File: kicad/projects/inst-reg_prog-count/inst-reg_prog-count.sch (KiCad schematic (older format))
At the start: 0 parts

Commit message: Place components in schematic.
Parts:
- added C? (x5): C, symbol Device:C
- added J?: Conn_01x34_Male, symbol Connector:Conn_01x34_Male
- added J? (x2): Conn_01x08_Female, symbol Connector:Conn_01x08_Female
- added J? (x2): Conn_01x16_Female, symbol Connector:Conn_01x16_Female
- added J?: Conn_01x08_Male, symbol Connector:Conn_01x08_Male
- added J? (x5): Conn_01x01_Female, symbol Connector:Conn_01x01_Female
- added U? (x2): 74HCT161, symbol eight-bit-computer:74HCT161
- added U?: 74HCT245, symbol eight-bit-computer:74HCT245
- added U? (x7): 74HCT04, symbol 74xx:74HCT04
- added U?: 74HCT377, symbol eight-bit-computer:74HCT377

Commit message: Almost finished PC IR schematic.
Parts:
- removed J?: Conn_01x08_Female, symbol Connector:Conn_01x08_Female
- removed J?: Conn_01x16_Female, symbol Connector:Conn_01x16_Female
- removed J?: Conn_01x01_Female, symbol Connector:Conn_01x01_Female
- added J?: Conn_01x08_Female, symbol Connector:Conn_01x08_Female
- added J?: Conn_01x16_Female, symbol Connector:Conn_01x16_Female
- added RN? (x2): R_Network08_US, Resistor_THT:R_Array_SIP9, symbol Device:R_Network08_US
- U?: value 74HCT161 -> 74HCT161 (LOW BITS)
- U?: value 74HCT161 -> 74HCT161 (HIGH BITS)
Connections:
- net at U?.1 (~MR): now also U?.1 (~MR), U?.4
- net at U?.10 (TE): now also C?.1, U?.16 (VCC)
- net at U?.11 (Q3): now also U?.5 (A3)
- net at U?.12 (Q2): now also U?.4 (A3)
- net at U?.13 (Q1): now also U?.3 (A2)
- net at U?.14 (Q0): now also U?.2 (A1)
- net at U?.15 (TC): now also U?.10 (TE)
- net BUS_0: now reaches U?.3 (P0)
- net BUS_0: now also J?.1 (Pin_1), U?.3 (D0)
- net BUS_1: now reaches U?.4 (P1)
- net BUS_1: now also J?.2 (Pin_2), U?.4 (D1)
- net BUS_2: now reaches U?.5 (P2)
- net BUS_2: now also J?.3 (Pin_3), U?.7 (D2)
- net BUS_3: now reaches U?.6 (P3)
- net BUS_3: now also J?.4 (Pin_4), U?.8 (D3)
- net PC_COUNT: now reaches U?.7 (PE)
- net PC_COUNT: now also U?.7 (PE)
- net at U?.8 (GND): now also C?.2 (x2)
- net at U?.9 (~SPE): now also U?.2, U?.9 (~SPE)
- net at U?.11 (Q3): now also U?.9 (A8)
- net at U?.12 (Q2): now also U?.8 (A7)
- net at U?.13 (Q1): now also U?.7 (A6)
- net at U?.14 (Q0): now also U?.6 (A5)
- net at U?.16 (VCC): now also C?.1
- net BUS_4: now reaches U?.3 (P0)
- net BUS_4: now also J?.5 (Pin_5), U?.13 (D4)
- net BUS_5: now reaches U?.4 (P1)
- net BUS_5: now also J?.6 (Pin_6), U?.14 (D5)
- net BUS_6: now reaches U?.5 (P2)
- net BUS_6: now also J?.7 (Pin_7), U?.17 (D6)
- net BUS_7: now reaches U?.6 (P3)
- net BUS_7: now also J?.8 (Pin_8), U?.18 (D7)
- net at U?.1 (DIR): now also C?.2, U?.10 (GND)
- net PC_7: now reaches U?.11 (B8)
- net PC_7: now also J?.1 (Pin_1), J?.15 (Pin_15)
- net PC_6: now reaches U?.12 (B7)
- net PC_6: now also J?.13 (Pin_13), J?.2 (Pin_2)
- net PC_5: now reaches U?.13 (B6)
- net PC_5: now also J?.11 (Pin_11), J?.3 (Pin_3)
- net PC_4: now reaches U?.14 (B5)
- net PC_4: now also J?.4 (Pin_4), J?.9 (Pin_9)
- net PC_3: now reaches U?.15 (B4)
- net PC_3: now also J?.5 (Pin_5), J?.7 (Pin_7)
- net PC_2: now reaches U?.16 (B3)
- net PC_2: now also J?.5 (Pin_5), J?.6 (Pin_6)
- net PC_1: now reaches U?.17 (B2)
- net PC_1: now also J?.3 (Pin_3), J?.7 (Pin_7)
- net PC_0: now reaches U?.18 (B1)
- net PC_0: now also J?.1 (Pin_1), J?.8 (Pin_8)
- net at U?.19 (~OE): now also U?.6
- net at U?.20 (VCC): now also C?.1 (x2)
- net PC_IN: now reaches U?.1
- net RESET: now reaches U?.3
- net PC_OUT: now reaches U?.5
- net at U?.1 (~E): now also C?.2, U?.10 (GND)
- net IR_4: now reaches U?.12 (Q4)
- net IR_4: now also J?.4 (Pin_4), J?.9 (Pin_9)
- net IR_5: now reaches U?.15 (Q5)
- net IR_5: now also J?.11 (Pin_11), J?.3 (Pin_3)
- net IR_6: now reaches U?.16 (Q6)
- net IR_6: now also J?.13 (Pin_13), J?.2 (Pin_2)
- net IR_7: now reaches U?.19 (Q7)
- net IR_7: now also J?.1 (Pin_1), J?.15 (Pin_15)
- net IR_0: now reaches U?.2 (Q0)
- net IR_0: now also J?.1 (Pin_1), J?.8 (Pin_8)
- net IR_1: now reaches U?.5 (Q1)
- net IR_1: now also J?.3 (Pin_3), J?.7 (Pin_7)
- net IR_2: now reaches U?.6 (Q2)
- net IR_2: now also J?.5 (Pin_5), J?.6 (Pin_6)
- net IR_3: now reaches U?.9 (Q3)
- net IR_3: now also J?.5 (Pin_5), J?.7 (Pin_7)
- net at J?.10 (Pin_10): now also RN?.6 (R5)
- net at J?.12 (Pin_12): now also RN?.7 (R6)
- net at J?.14 (Pin_14): now also RN?.8 (R7)
- net at J?.16 (Pin_16): now also RN?.9 (R8)
- net at J?.2 (Pin_2): now also RN?.2 (R1)
- net at J?.4 (Pin_4): now also RN?.3 (R2)
- net at J?.6 (Pin_6): now also RN?.4 (R3)
- net at J?.8 (Pin_8): now also RN?.5 (R4)
- new net: J?.10 (Pin_10), RN?.6 (R5)
- new net: J?.12 (Pin_12), RN?.7 (R6)
- new net: J?.14 (Pin_14), RN?.8 (R7)
- new net: J?.16 (Pin_16), RN?.9 (R8)
- new net: J?.2 (Pin_2), RN?.2 (R1)
- new net: J?.4 (Pin_4), RN?.3 (R2)
- new net: J?.6 (Pin_6), RN?.4 (R3)
- new net: J?.8 (Pin_8), RN?.5 (R4)
- no-connect marks 0 -> 1
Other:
- moved on the sheet: C?, J?, U?, U?A, U?B, U?C, U?D, U?E, U?F, U?G

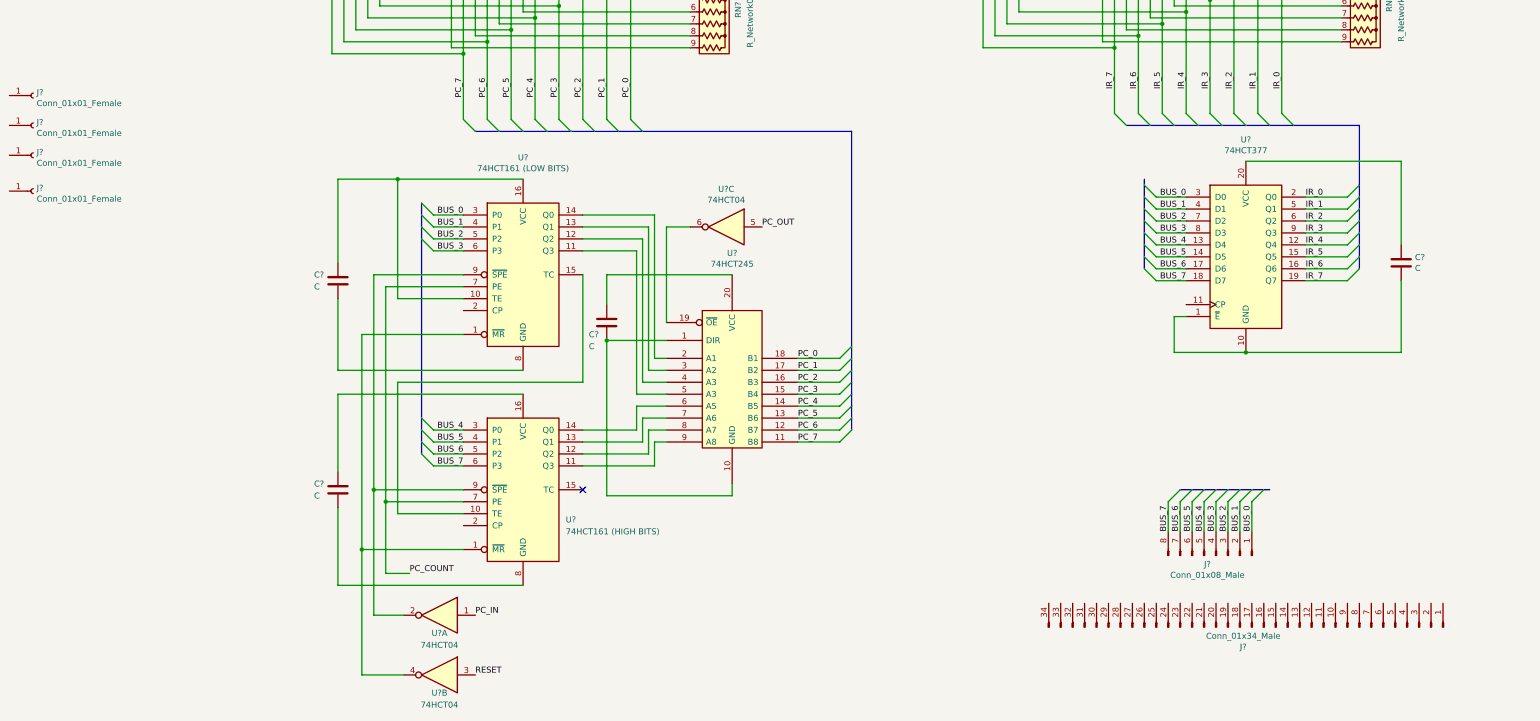
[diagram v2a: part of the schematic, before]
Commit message: Add bacplane to symbol library
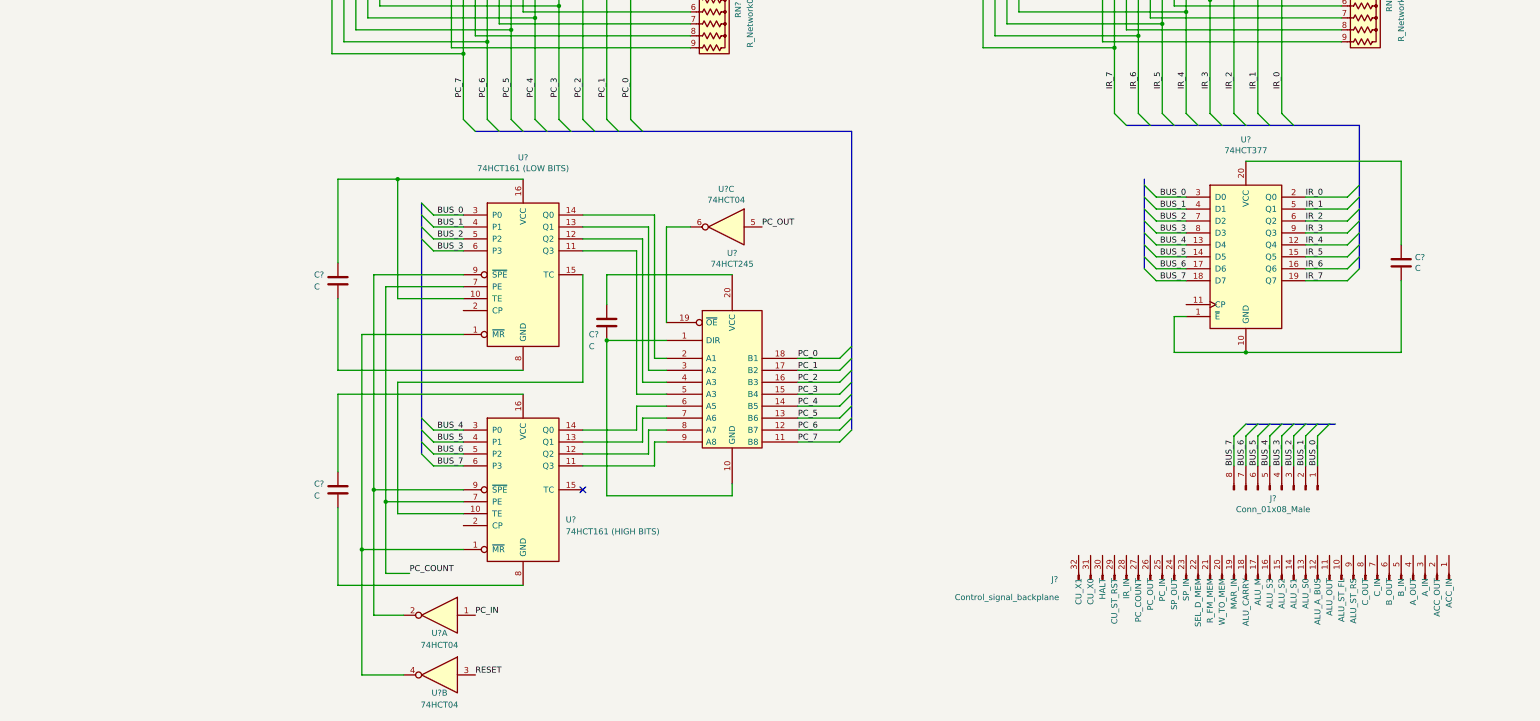
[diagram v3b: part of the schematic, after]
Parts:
- removed J?: Conn_01x34_Male, symbol Connector:Conn_01x34_Male
- removed J? (x4): Conn_01x01_Female, symbol Connector:Conn_01x01_Female
- added J?: Control_signal_backplane, symbol eight-bit-computer:Control_signal_backplane
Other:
- moved on the sheet: J?
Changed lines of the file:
@@
-$EndComp
-$Comp
-L Connector:Conn_01x34_Male J?
-U 1 1 5F5EFDF6
-P 8550 6600
-F 0 "J?" V 8385 6528 50  0000 C CNN
-F 1 "Conn_01x34_Male" V 8476 6528 50  0000 C CNN
-F 2 "" H 8550 6600 50  0001 C CNN
-F 3 "~" H 8550 6600 50  0001 C CNN
-	1    8550 6600
-	0    1    -1   0
 $EndComp
 $Comp
@@
 L Connector:Conn_01x08_Male J?
 U 1 1 5F628213
-P 8250 6000
-F 0 "J?" V 8177 5928 50  0000 C CNN
-F 1 "Conn_01x08_Male" V 8086 5928 50  0000 C CNN
-F 2 "" H 8250 6000 50  0001 C CNN
-F 3 "~" H 8250 6000 50  0001 C CNN
-	1    8250 6000
+P 8800 5450
+F 0 "J?" V 8727 5378 50  0000 C CNN
+F 1 "Conn_01x08_Male" V 8636 5378 50  0000 C CNN
+F 2 "" H 8800 5450 50  0001 C CNN
+F 3 "~" H 8800 5450 50  0001 C CNN
+	1    8800 5450
 	0    1    -1   0
-$EndComp
-$Comp
-L Connector:Conn_01x01_Female J?
-U 1 1 5F6429BE
-P -1650 2650
-F 0 "J?" H -1622 2676 50  0000 L CNN
-F 1 "Conn_01x01_Female" H -1622 2585 50  0000 L CNN
-F 2 "" H -1650 2650 50  0001 C CNN
-F 3 "~" H -1650 2650 50  0001 C CNN
-	1    -1650 2650
-	1    0    0    -1
-$EndComp
-$Comp
-L Connector:Conn_01x01_Female J?
-U 1 1 5F643E35
-P -1650 2950
-F 0 "J?" H -1622 2976 50  0000 L CNN
-F 1 "Conn_01x01_Female" H -1622 2885 50  0000 L CNN
-F 2 "" H -1650 2950 50  0001 C CNN
-F 3 "~" H -1650 2950 50  0001 C CNN
-	1    -1650 2950
-	1    0    0    -1
-$EndComp
-$Comp
-L Connector:Conn_01x01_Female J?
-U 1 1 5F644FE4
-P -1650 2400
-F 0 "J?" H -1622 2426 50  0000 L CNN
-F 1 "Conn_01x01_Female" H -1622 2335 50  0000 L CNN
-F 2 "" H -1650 2400 50  0001 C CNN
-F 3 "~" H -1650 2400 50  0001 C CNN
-	1    -1650 2400
-	1    0    0    -1
-$EndComp
-$Comp
-L Connector:Conn_01x01_Female J?
-U 1 1 5F645644
-P -1650 2150
-F 0 "J?" H -1622 2176 50  0000 L CNN
-F 1 "Conn_01x01_Female" H -1622 2085 50  0000 L CNN
-F 2 "" H -1650 2150 50  0001 C CNN
-F 3 "~" H -1650 2150 50  0001 C CNN
-	1    -1650 2150
-	1    0    0    -1
 $EndComp
 $Comp
@@
 	0    1    1    0
 $EndComp
-Text Label 8550 5800 1    50   ~ 0
+Text Label 9100 5250 1    50   ~ 0
 BUS_0
-Text Label 7950 5800 1    50   ~ 0
+Text Label 8500 5250 1    50   ~ 0
 BUS_6
-Text Label 8050 5800 1    50   ~ 0
+Text Label 8600 5250 1    50   ~ 0
 BUS_5
-Text Label 8150 5800 1    50   ~ 0
+Text Label 8700 5250 1    50   ~ 0
 BUS_4
-Text Label 8250 5800 1    50   ~ 0
+Text Label 8800 5250 1    50   ~ 0
 BUS_3
-Text Label 8350 5800 1    50   ~ 0
+Text Label 8900 5250 1    50   ~ 0
 BUS_2
-Text Label 8450 5800 1    50   ~ 0
+Text Label 9000 5250 1    50   ~ 0
 BUS_1
-Text Label 7850 5800 1    50   ~ 0
+Text Label 8400 5250 1    50   ~ 0
 BUS_7
 Wire Wire Line
-	7850 5800 7850 5550
-Wire Wire Line
-	7950 5800 7950 5550
-Wire Wire Line
-	8050 5800 8050 5550
-Wire Wire Line
-	8150 5800 8150 5550
-Wire Wire Line
-	8250 5800 8250 5550
-Wire Wire Line
-	8350 5800 8350 5550
-Wire Wire Line
-	8450 5800 8450 5550
-Wire Wire Line
-	8550 5800 8550 5550
-Entry Wire Line
-	7850 5550 7950 5450
-Entry Wire Line
-	7950 5550 8050 5450
-Entry Wire Line
-	8050 5550 8150 5450
-Entry Wire Line
-	8150 5550 8250 5450
-Entry Wire Line
-	8250 5550 8350 5450
-Entry Wire Line
-	8350 5550 8450 5450
-Entry Wire Line
-	8450 5550 8550 5450
-Entry Wire Line
-	8550 5550 8650 5450
+	8400 5250 8400 5000
+Wire Wire Line
+	8500 5250 8500 5000
+Wire Wire Line
+	8600 5250 8600 5000
+Wire Wire Line
+	8700 5250 8700 5000
+Wire Wire Line
+	8800 5250 8800 5000
+Wire Wire Line
+	8900 5250 8900 5000
+Wire Wire Line
+	9000 5250 9000 5000
+Wire Wire Line
+	9100 5250 9100 5000
+Entry Wire Line
+	8400 5000 8500 4900
+Entry Wire Line
+	8500 5000 8600 4900
+Entry Wire Line
+	8600 5000 8700 4900
+Entry Wire Line
+	8700 5000 8800 4900
+Entry Wire Line
+	8800 5000 8900 4900
+Entry Wire Line
+	8900 5000 9000 4900
+Entry Wire Line
+	9000 5000 9100 4900
+Entry Wire Line
+	9100 5000 9200 4900
 Text Label 8000 3000 2    50   ~ 0
 BUS_0
@@
 Entry Wire Line
 	3350 2350 3450 2450
+$Comp
+L eight-bit-computer:Control_signal_backplane J?
+U 1 1 5FC65F18
+P 8700 6200
+F 0 "J?" V 8700 4400 50  0000 C CNN
+F 1 "Control_signal_backplane" V 8550 4000 50  0000 C CNN
+F 2 "" H 8700 6200 50  0001 C CNN
+F 3 "~" H 8700 6200 50  0001 C CNN
+	1    8700 6200
+	0    1    -1   0
+$EndComp
 Wire Bus Line
 	1600 3050 1600 5150
@@
 	7650 2850 7650 3600
 Wire Bus Line
-	7950 5450 8700 5450
+	8500 4900 9250 4900
 $EndSCHEMATC

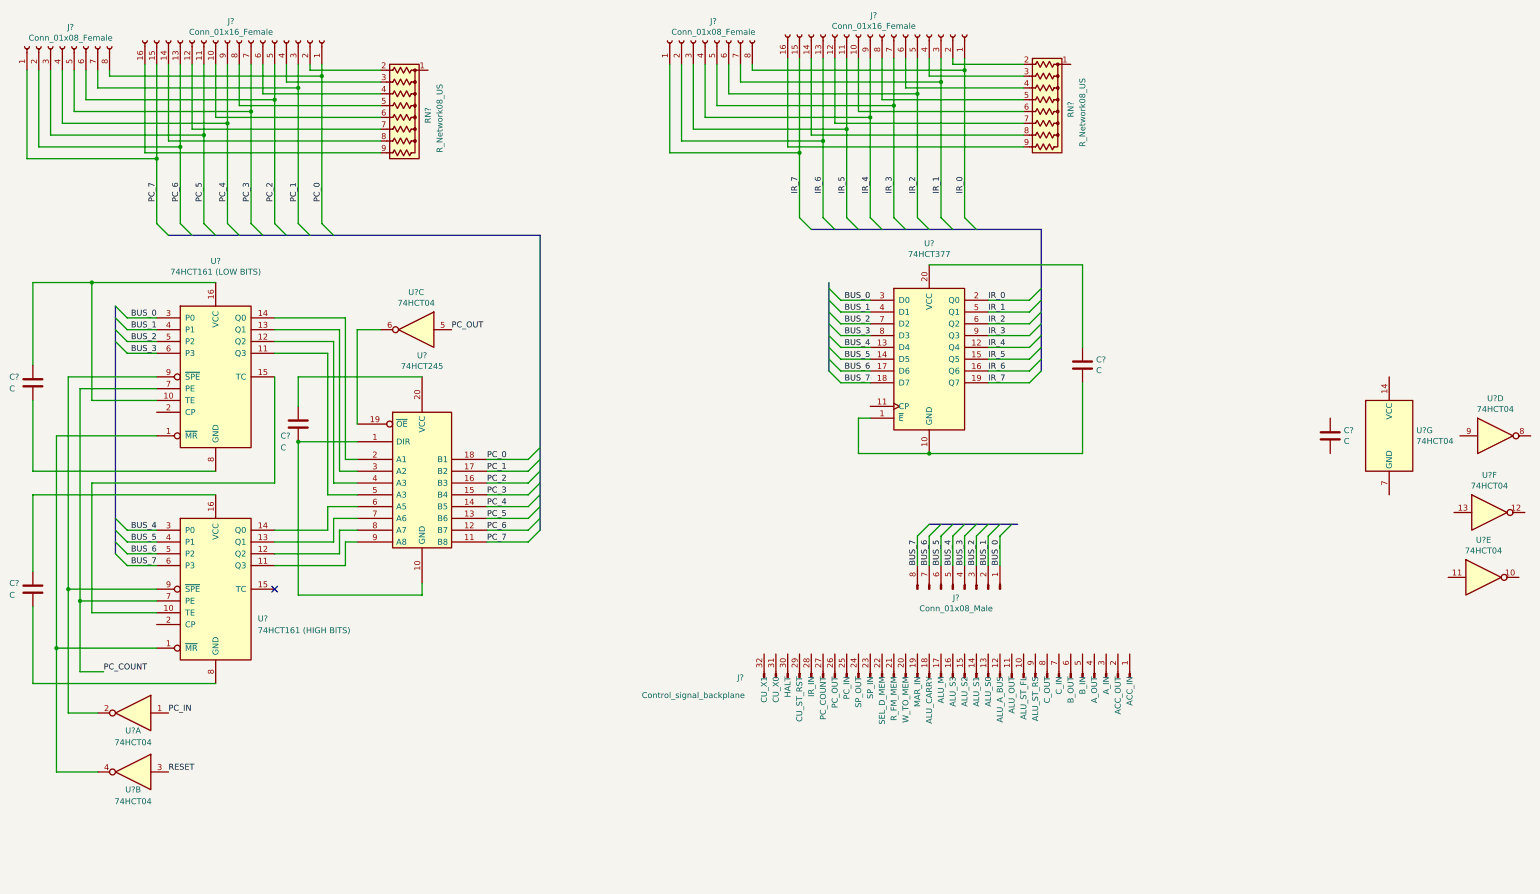
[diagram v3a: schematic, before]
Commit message: Add connectors to shared libs. Updates to use new connectors.
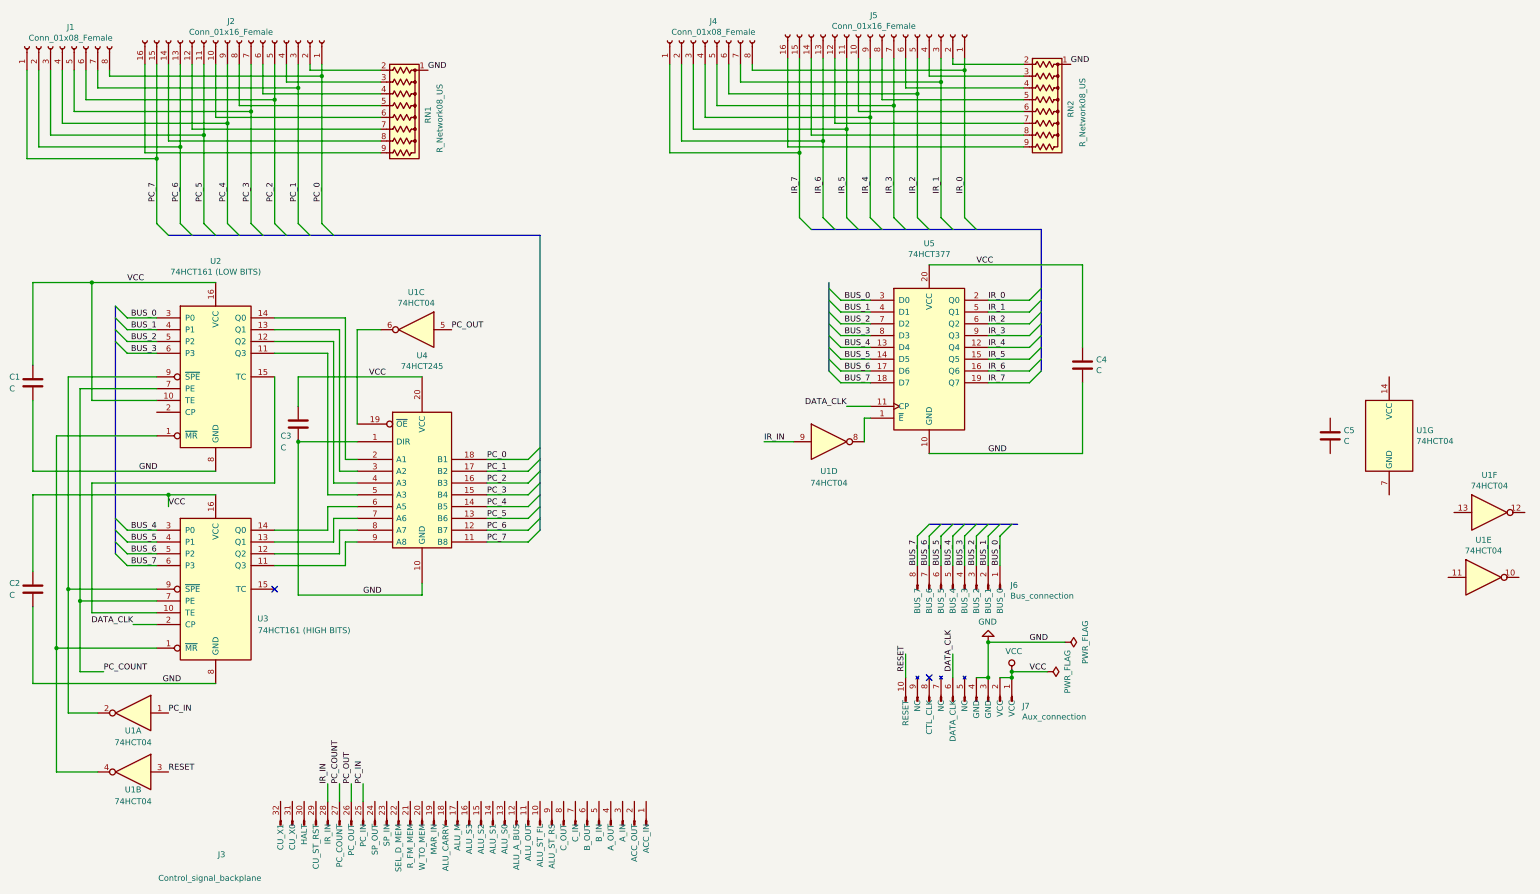
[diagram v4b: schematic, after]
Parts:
- removed J?: Conn_01x08_Male, symbol Connector:Conn_01x08_Male
- removed J?: Control_signal_backplane, symbol eight-bit-computer:Control_signal_backplane
- added J3: Control_signal_backplane, symbol eight-bit-computer:Control_signal_backplane
- added J6: Bus_connection, symbol eight-bit-computer:Bus_connection
- added J7: Aux_connection, symbol eight-bit-computer:Aux_connection
- gave numbers to parts that had none: 16
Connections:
- net BUS_0: now also J6.1 (BUS_0)
- net BUS_1: now also J6.2 (BUS_1)
- net BUS_2: now also J6.3 (BUS_2)
- net BUS_3: now also J6.4 (BUS_3)
- net BUS_4: now also J6.5 (BUS_4)
- net BUS_5: now also J6.6 (BUS_5)
- net BUS_6: now also J6.7 (BUS_6)
- net BUS_7: now also J6.8 (BUS_7)
- net PC_COUNT: now also J3.27 (PC_COUNT)
- net PC_IN: now also J3.25 (PC_IN)
- net PC_OUT: now also J3.26 (PC_OUT)
- net RESET: now also J7.10 (RESET)
- net VCC: now reaches C1.1, U2.10 (TE), U2.16 (VCC)
- net VCC: now also C2.1, C3.1, C4.1, U3.16 (VCC), U4.20 (VCC), U5.20 (VCC), J7.1 (VCC), J7.2 (VCC)
- net GND: now reaches C1.2, U2.8 (GND)
- net GND: now also C2.2, C3.2, C4.2, RN1.1 (common), RN2.1 (common), U3.8 (GND), U4.1 (DIR), U4.10 (GND), U5.10 (GND), J7.3 (GND), J7.4 (GND)
- net DATA_CLK: now reaches U3.2 (CP)
- net DATA_CLK: now also U5.11 (CP), J7.6 (DATA_CLK)
- net at U1.8: now also U5.1 (~E)
- net IR_IN: now reaches U1.9
- net IR_IN: now also J3.28 (IR_IN)
- no-connect marks 1 -> 2
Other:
- moved on the sheet: U1D
